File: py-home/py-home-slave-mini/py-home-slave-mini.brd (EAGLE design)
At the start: 48.2 x 72.1 mm, 20 parts, among them IC1 uln2308, K1 JS-M1-9V-4, K2 JS-M1-9V-4

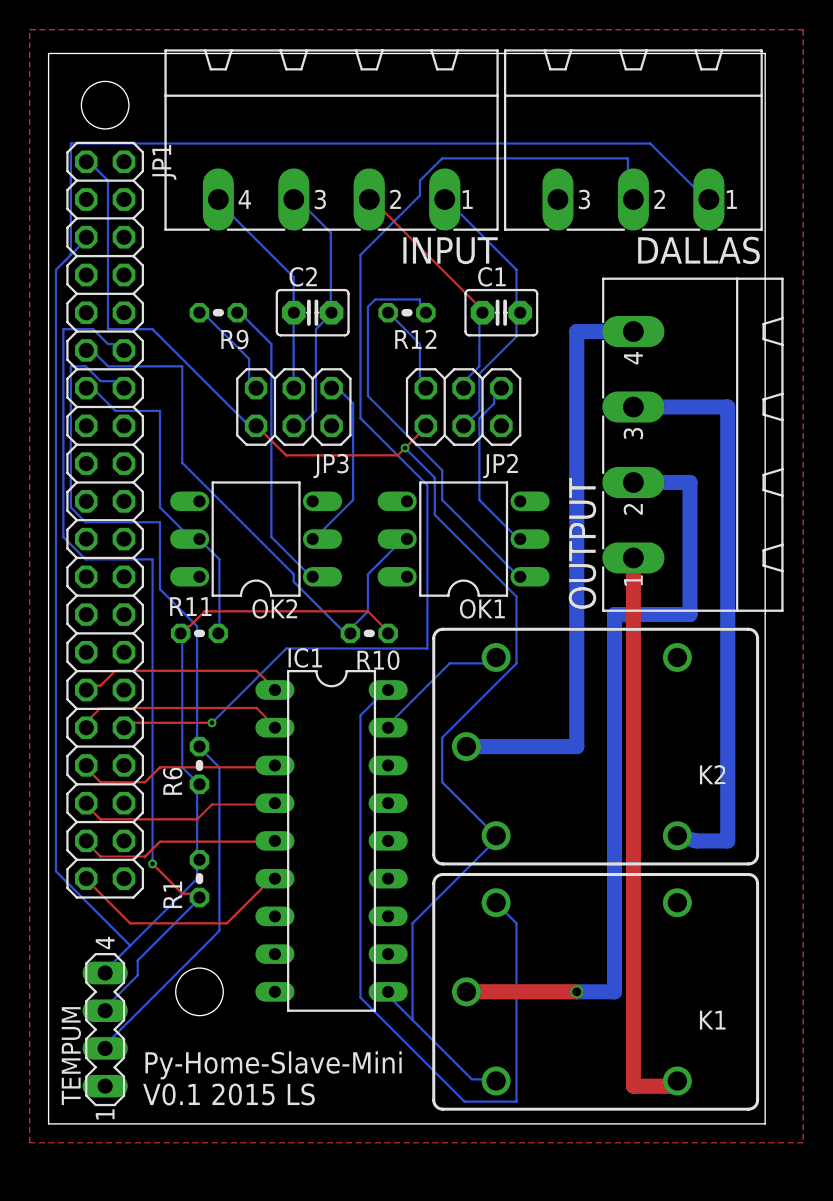
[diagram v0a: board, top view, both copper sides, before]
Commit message: aggiunto porta usb
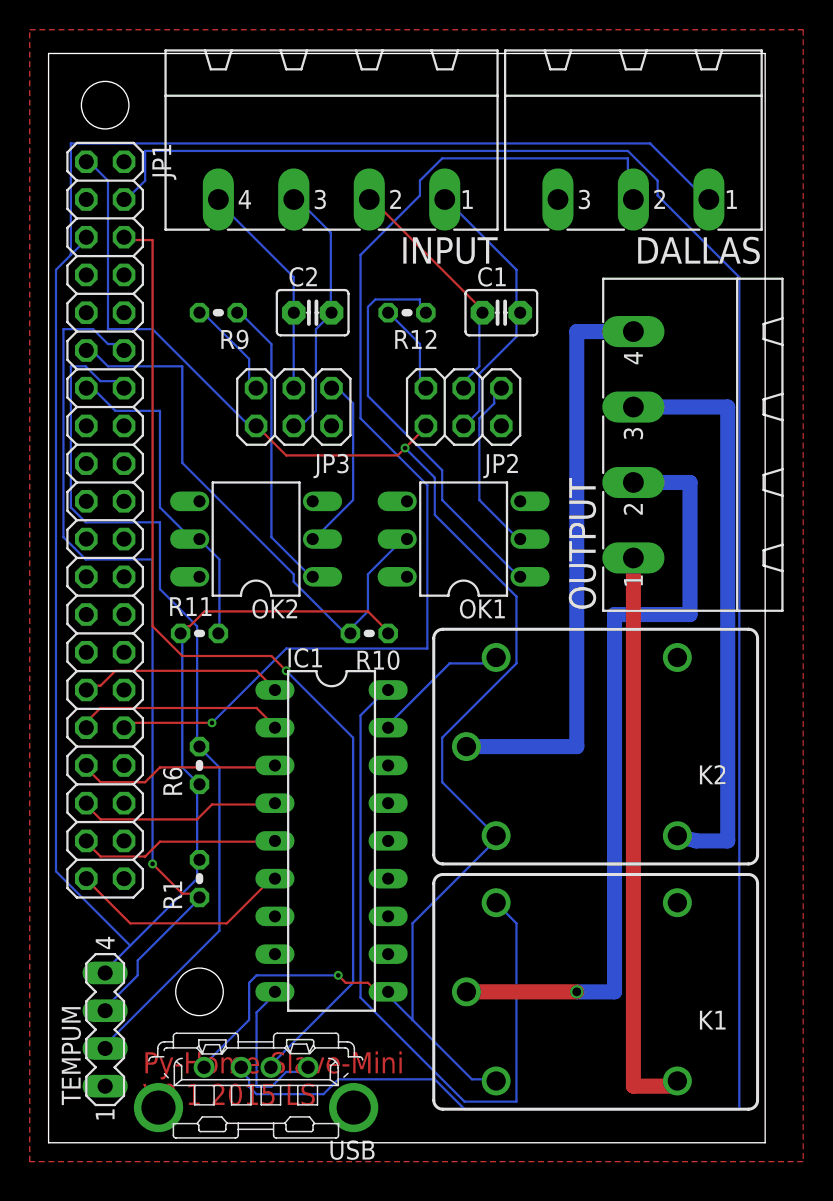
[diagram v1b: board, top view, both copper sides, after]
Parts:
- added USB: KUSBVX, con-kycon:KUSBVX
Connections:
- net 5V: now also USB.1
- net GND: now also USB.4
- net USBAD+: now also USB.3
- net USBAD-: now also USB.2
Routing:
- net USBAD-: track 0.00 -> 140.0 mm
- net USBAD+: track 0.00 -> 69.0 mm, vias 0 -> 1
- net 5V: track 95.3 -> 112.3 mm, vias 1 -> 2
- net GND: track 0.00 -> 10.8 mm
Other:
- board size 48.2 x 72.1 mm -> 48.2 x 73.3 mm
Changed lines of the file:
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@@
 <board>
 <plain>
-<wire x1="0" y1="0" x2="48.24" y2="0" width="0" layer="20"/>
-<wire x1="48.24" y1="0" x2="48.24" y2="72.06" width="0" layer="20"/>
+<wire x1="0" y1="-1.27" x2="48.24" y2="-1.27" width="0" layer="20"/>
+<wire x1="48.24" y1="-1.27" x2="48.24" y2="72.06" width="0" layer="20"/>
 <wire x1="48.24" y1="72.06" x2="0" y2="72.06" width="0" layer="20"/>
-<wire x1="0" y1="72.06" x2="0" y2="0" width="0" layer="20"/>
-<text x="6.35" y="1.27" size="1.4224" layer="21">Py-Home-Slave-Mini
+<wire x1="0" y1="72.06" x2="0" y2="-1.27" width="0" layer="20"/>
+<text x="6.35" y="1.27" size="1.4224" layer="1">Py-Home-Slave-Mini
 V0.1 2015 LS</text>
 <hole x="3.81" y="68.58" drill="3.2"/>
@@
 <description language="de">&lt;b&gt;EAGLE Design Rules&lt;/b&gt;
 &lt;p&gt;
-Die Standard-Design-Rules sind so gewählt, dass sie für
+Die Standard-Design-Rules sind so gewÃ¤hlt, dass sie fÃ¼r
 die meisten Anwendungen passen. Sollte ihre Platine
 besondere Anforderungen haben, treffen Sie die erforderlichen
@@
 <attribute name="OC_FARNELL" value="3705195" x="44.45" y="45.72" size="1.778" layer="27" rot="R90" display="off"/>
 </element>
+<element name="USB" library="con-kycon" package="KUSBVX" value="KUSBVX" x="13.97" y="3.81" rot="R180"/>
 </elements>
 <signals>
@@
 <wire x1="30" y1="19.5" x2="30.13" y2="19.4" width="0.1524" layer="16"/>
 <via x="24" y="45.5" extent="1-16" drill="0.3048"/>
+<contactref element="USB" pad="1"/>
+<wire x1="13.5" y1="7" x2="10.5" y2="4" width="0.1524" layer="16"/>
+<wire x1="13.5" y1="9.5" x2="13.5" y2="7" width="0.1524" layer="16"/>
+<wire x1="14" y1="10" x2="13.5" y2="9.5" width="0.1524" layer="16"/>
+<wire x1="19.5" y1="10" x2="14" y2="10" width="0.1524" layer="16"/>
+<wire x1="20" y1="9.5" x2="19.5" y2="10" width="0.1524" layer="1"/>
+<wire x1="21.5" y1="9.5" x2="20" y2="9.5" width="0.1524" layer="1"/>
+<wire x1="22" y1="9" x2="21.5" y2="9.5" width="0.1524" layer="1"/>
+<wire x1="22.5" y1="9" x2="22" y2="9" width="0.1524" layer="1"/>
+<wire x1="10.5" y1="4" x2="10.47" y2="3.81" width="0.1524" layer="16"/>
+<wire x1="22.5" y1="9" x2="22.86" y2="8.89" width="0.1524" layer="1"/>
+<via x="19.5" y="10" extent="1-16" drill="0.3048"/>
 </signal>
 <signal name="VBAT">
@@
 <signal name="USBAD+">
 <contactref element="JP1" pad="6"/>
+<contactref element="USB" pad="3"/>
+<wire x1="20.5" y1="9.5" x2="15" y2="4" width="0.1524" layer="16"/>
+<wire x1="20.5" y1="26" x2="20.5" y2="9.5" width="0.1524" layer="16"/>
+<wire x1="16" y1="30.5" x2="20.5" y2="26" width="0.1524" layer="16"/>
+<wire x1="15" y1="31.5" x2="16" y2="30.5" width="0.1524" layer="1"/>
+<wire x1="9" y1="31.5" x2="15" y2="31.5" width="0.1524" layer="1"/>
+<wire x1="7" y1="33.5" x2="9" y2="31.5" width="0.1524" layer="1"/>
+<wire x1="7" y1="59.5" x2="7" y2="33.5" width="0.1524" layer="1"/>
+<wire x1="5.5" y1="59.5" x2="7" y2="59.5" width="0.1524" layer="1"/>
+<wire x1="15" y1="4" x2="14.97" y2="3.81" width="0.1524" layer="16"/>
+<wire x1="5.5" y1="59.5" x2="5.08" y2="59.69" width="0.1524" layer="1"/>
+<via x="16" y="30.5" extent="1-16" drill="0.3048"/>
 </signal>
 <signal name="USBAD-">
 <contactref element="JP1" pad="4"/>
+<contactref element="USB" pad="2"/>
+<wire x1="13.5" y1="3" x2="13" y2="3.5" width="0.1524" layer="16"/>
+<wire x1="13.5" y1="2.5" x2="13.5" y2="3" width="0.1524" layer="16"/>
+<wire x1="14" y1="2" x2="13.5" y2="2.5" width="0.1524" layer="16"/>
+<wire x1="18.5" y1="2" x2="14" y2="2" width="0.1524" layer="16"/>
+<wire x1="19.5" y1="3" x2="18.5" y2="2" width="0.1524" layer="16"/>
+<wire x1="26" y1="3" x2="19.5" y2="3" width="0.1524" layer="16"/>
+<wire x1="28" y1="1" x2="26" y2="3" width="0.1524" layer="16"/>
+<wire x1="46.5" y1="1" x2="28" y2="1" width="0.1524" layer="16"/>
+<wire x1="46.5" y1="57" x2="46.5" y2="1" width="0.1524" layer="16"/>
+<wire x1="41" y1="62.5" x2="46.5" y2="57" width="0.1524" layer="16"/>
+<wire x1="41" y1="63.5" x2="41" y2="62.5" width="0.1524" layer="16"/>
+<wire x1="39" y1="65.5" x2="41" y2="63.5" width="0.1524" layer="16"/>
+<wire x1="6.5" y1="65.5" x2="39" y2="65.5" width="0.1524" layer="16"/>
+<wire x1="6.5" y1="63.5" x2="6.5" y2="65.5" width="0.1524" layer="16"/>
+<wire x1="5.5" y1="62.5" x2="6.5" y2="63.5" width="0.1524" layer="16"/>
+<wire x1="13" y1="3.5" x2="12.97" y2="3.81" width="0.1524" layer="16"/>
+<wire x1="5.5" y1="62.5" x2="5.08" y2="62.23" width="0.1524" layer="16"/>
 </signal>
 <signal name="O6">
@@
 <vertex x="-1.27" y="73.66"/>
 <vertex x="50.8" y="73.66"/>
-<vertex x="50.8" y="-1.27"/>
-<vertex x="-1.27" y="-1.27"/>
+<vertex x="50.8" y="-2.54"/>
+<vertex x="-1.27" y="-2.54"/>
 </polygon>
 <contactref element="IC1" pad="9"/>
@@
 <contactref element="JP2" pad="2"/>
 <contactref element="JP3" pad="2"/>
+<contactref element="USB" pad="4"/>
+<wire x1="16" y1="3.5" x2="17" y2="3.5" width="0.1524" layer="16"/>
+<wire x1="15" y1="2.5" x2="16" y2="3.5" width="0.1524" layer="16"/>
+<wire x1="14" y1="2.5" x2="15" y2="2.5" width="0.1524" layer="16"/>
+<wire x1="14" y1="7.5" x2="14" y2="2.5" width="0.1524" layer="16"/>
+<wire x1="15" y1="8.5" x2="14" y2="7.5" width="0.1524" layer="16"/>
+<wire x1="17" y1="3.5" x2="17.47" y2="3.81" width="0.1524" layer="16"/>
+<wire x1="15" y1="8.5" x2="15.24" y2="8.89" width="0.1524" layer="16"/>
 </signal>
 <signal name="N$25">
